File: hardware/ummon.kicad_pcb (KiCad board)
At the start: 4 copper layers, 60 x 60 mm, 84 parts, among them J1 Conn_01x08_Pin, J2 Conn_01x05_Pin, J3 Conn_01x04_Pin, J4 Conn_01x04_Pin, J5 Conn_01x04_Pin, P1 FPC 0.5MM 24P Vertical, Q1 SI1308EDL, SW1 Reboot, SW2 Flash, SW3 Test Button, U1 ESP32-C6-WROOM-1-N8, U2 SCD41-D-R2, U3 SGP41-D-R4, U4 SHT41-AD1B-R2, U5 AMS1117-3.3, U7 SMBJ6.5CA

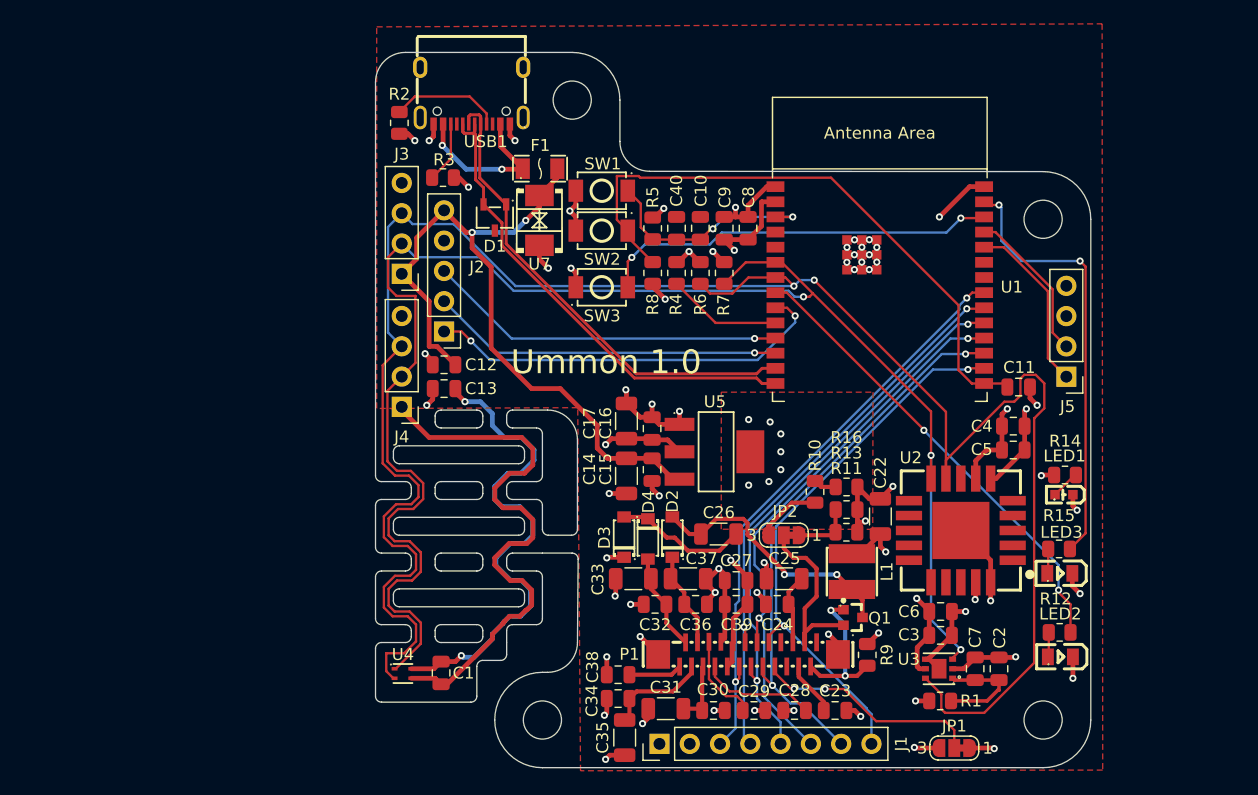
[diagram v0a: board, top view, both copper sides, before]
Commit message: :construction: WIP place ESD parts and route epd charge pump
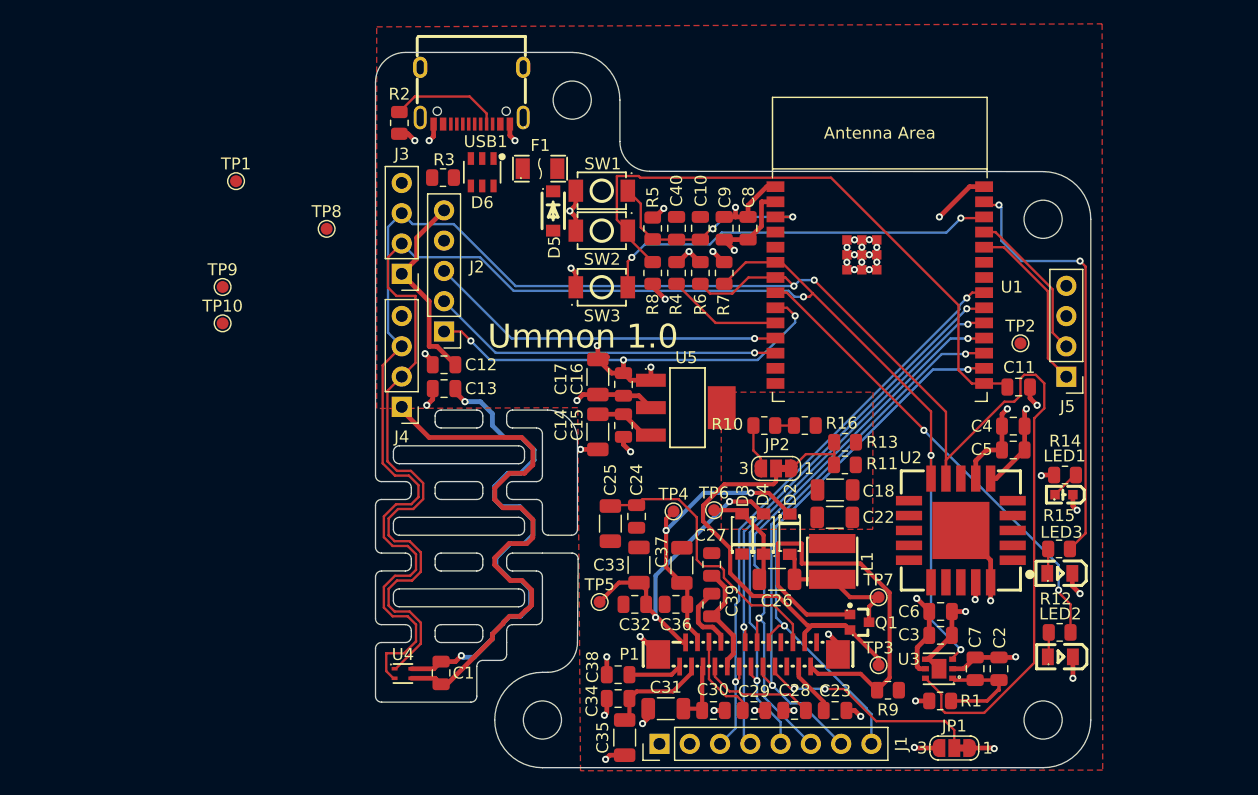
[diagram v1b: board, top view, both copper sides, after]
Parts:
- removed D1: PSM712-LF-T7, parts:SOT-23-3_L3.0-W1.7-P0.95-LS2.9-BR
- removed U7: SMBJ6.5CA, parts:SMB_L4.6-W3.5-LS5.3-BI
- added C18: 22µF, Capacitor_SMD:C_1206_3216Metric, F.Cu at (153.6, 126.7)
- added D5: SMF5.0A, parts:SOD-123F_L2.8-W1.8-LS3.7-RD, F.Cu at (129.9, 103.3)
- added D6: USBLC6-2SC6, parts:SOT-23-6_L2.9-W1.6-P0.95-LS2.8-BL, F.Cu at (124.0, 100.0)
- added TP1: TestPoint, TestPoint:TestPoint_Pad_D1.0mm, F.Cu at (103.3, 100.8)
- added TP10: TestPoint, TestPoint:TestPoint_Pad_D1.0mm, F.Cu at (102.2, 112.7)
- added TP2: TestPoint, TestPoint:TestPoint_Pad_D1.0mm, F.Cu at (169.1, 114.4)
- added TP3: TestPoint, TestPoint:TestPoint_Pad_D1.0mm, F.Cu at (157.2, 141.4)
- added TP4: TestPoint, TestPoint:TestPoint_Pad_D1.0mm, F.Cu at (140.0, 128.5)
- added TP5: TestPoint, TestPoint:TestPoint_Pad_D1.0mm, F.Cu at (133.8, 136.1)
- added TP6: TestPoint, TestPoint:TestPoint_Pad_D1.0mm, F.Cu at (143.4, 128.4)
- added TP7: TestPoint, TestPoint:TestPoint_Pad_D1.0mm, F.Cu at (157.2, 135.7)
- added TP8: TestPoint, TestPoint:TestPoint_Pad_D1.0mm, F.Cu at (110.9, 104.8)
- added TP9: TestPoint, TestPoint:TestPoint_Pad_D1.0mm, F.Cu at (102.2, 109.7)
- moved C25 15.3 mm to (134.7, 129.5), turned to 90 degrees
- moved C24 13.9 mm to (136.9, 128.9), turned to 90 degrees
- moved D3 9.90 mm to (145.8, 130.4)
- moved D2 9.85 mm to (149.8, 130.4), turned to -90 degrees
- moved D4 9.71 mm to (147.6, 130.4), turned to 90 degrees
- moved R10 7.00 mm to (147.6, 121.3), turned to 180 degrees
- moved R16 6.23 mm to (151.0, 121.3)
- moved C26 6.20 mm to (148.7, 134.2), turned to 0 degrees
- moved R11 5.65 mm to (154.4, 124.6)
- moved R13 5.65 mm to (154.4, 122.7)
- moved JP2 5.64 mm to (148.6, 124.9)
- moved C14 4.41 mm to (133.7, 121.8)
- moved C17 4.41 mm to (133.7, 117.2)
- moved U5 4.41 mm to (141.1, 119.8)
- moved C15 4.41 mm to (135.8, 121.3)
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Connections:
- net Net-(D2-A) renamed /EPD_VGH
- net Net-(D3-A) renamed /EPD_VGL
- net Net-(F1-Pad1) renamed /USB_VBUS
- R2 pad 1: Net-(USB1-CC1) -> /USB_CC2
- R3 pad 1: Net-(USB1-CC2) -> /USB_CC1
- USB1 pad A5: Net-(USB1-CC1) -> /USB_CC1
- USB1 pad A6: /USB_D+ -> Net-(USB1-Dp1)
- USB1 pad A7: /USB_D- -> Net-(USB1-Dn1)
- USB1 pad B5: Net-(USB1-CC2) -> /USB_CC2
- USB1 pad B6: /USB_D+ -> Net-(USB1-Dp1)
- USB1 pad B7: /USB_D- -> Net-(USB1-Dn1)
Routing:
- net /USB_D+: track 41.3 -> 0.00 mm
- net /USB_D-: track 40.7 -> 0.00 mm
- net +5V: track 62.0 -> 21.8 mm, vias 2 -> 0
- net GND: track 159.6 -> 134.4 mm, vias 58 -> 46
- net /EPD_GDR: track 12.5 -> 37.7 mm, vias 2 -> 0
- net /EPD_RESE: track 15.5 -> 35.1 mm
- net /EPD_PREVGL: track 8.30 -> 26.3 mm, vias 0 -> 2
- net Net-(C24-Pad2): track 5.93 -> 23.9 mm
- net /EPD_PREVGH: track 8.13 -> 24.7 mm, vias 0 -> 2
- net /USB_VBUS: track 13.9 -> 0.00 mm, vias 2 -> 0
- net /EPD_VGH: track 22.1 -> 12.4 mm, vias 2 -> 0
- net Net-(USB1-CC1): track 9.34 -> 0.00 mm
- net (no net): track 0.00 -> 9.34 mm
- net +3.3V: track 106.7 -> 101.5 mm, vias 22 -> 13
- net Net-(USB1-CC2): track 5.14 -> 0.00 mm
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
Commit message: :zap: Adjust I2C routing between header and SHT41
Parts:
- moved TP1 28.9 mm to (132.1, 99.1)
- moved D6 4.97 mm to (127.2, 103.8)
- moved TP3 1.35 mm to (156.9, 140.1)
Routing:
- net +3.3V: track 101.5 -> 106.3 mm
- net GND: track 134.4 -> 139.1 mm
- net /EPD_RESE: track 35.1 -> 31.2 mm
- net /I2C_SDA: track 133.2 -> 136.3 mm
- net /I2C_SCL: track 170.4 -> 172.5 mm

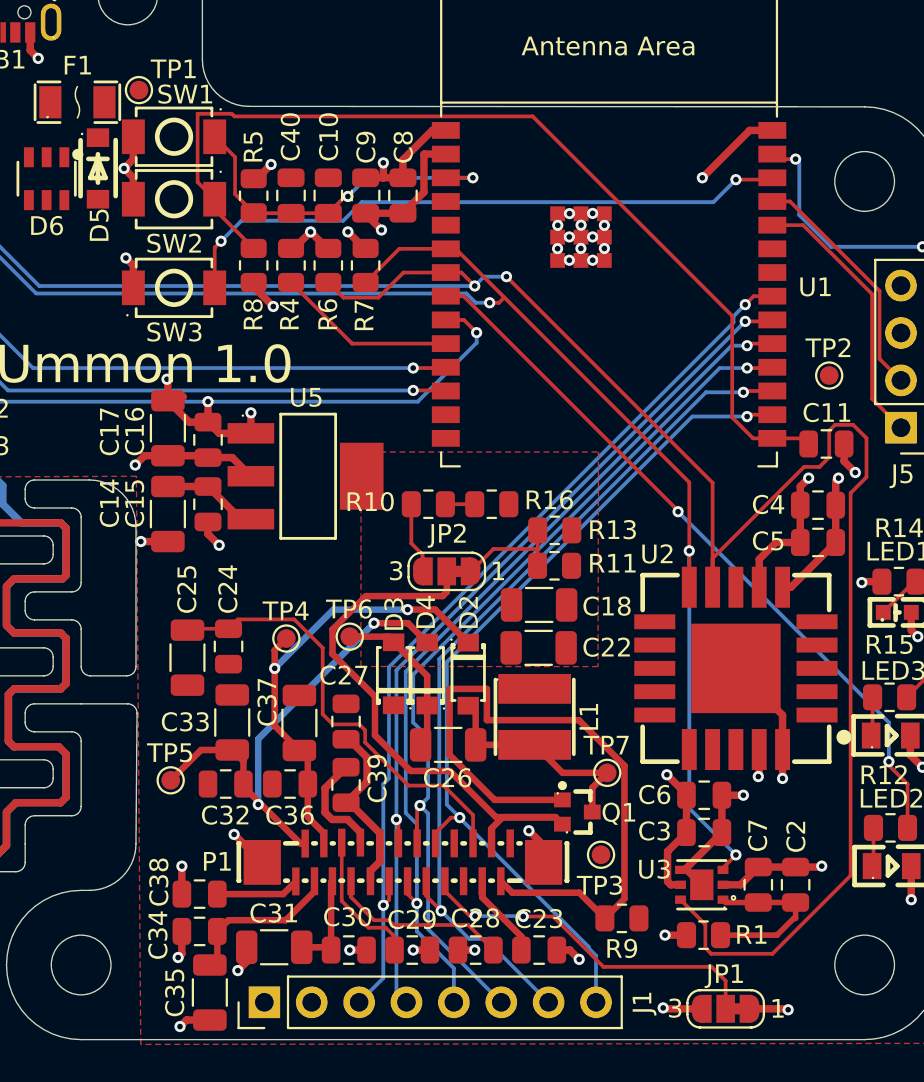
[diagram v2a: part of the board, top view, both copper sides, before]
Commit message: :zap: Rework EPD routing around display connector
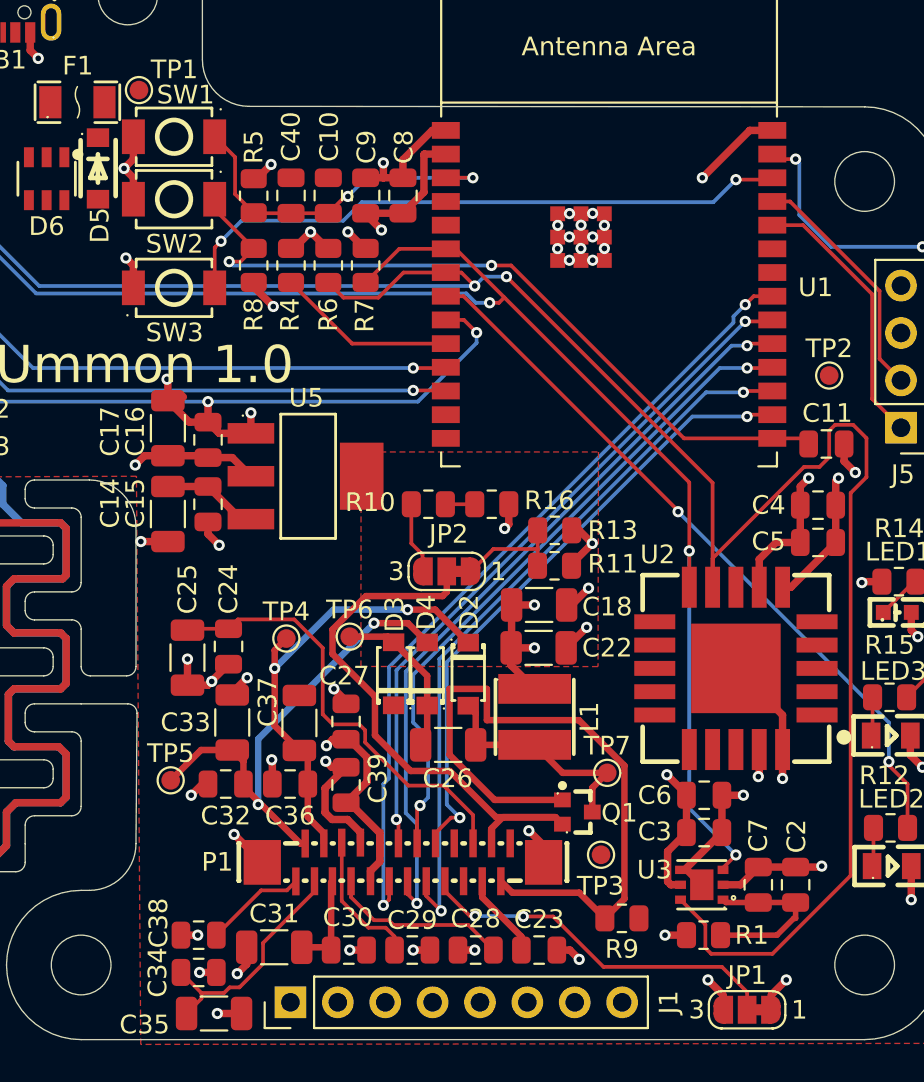
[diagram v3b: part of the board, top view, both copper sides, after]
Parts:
- moved C34 2.20 mm to (135.3, 146.4), turned to 180 degrees
- moved C38 2.20 mm to (135.3, 144.4)
- moved J1 1.40 mm to (140.2, 148.0)
- moved JP1 1.15 mm to (164.7, 148.4)
- moved C35 1.15 mm to (136.1, 148.6), turned to 180 degrees
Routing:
- net GND: track 139.1 -> 155.1 mm, vias 46 -> 57
- net /GPIO9: track 51.7 -> 40.2 mm, vias 0 -> 2
- net +3.3V: track 106.3 -> 114.9 mm, vias 13 -> 16
- net Net-(C34-Pad2): track 8.61 -> 12.5 mm
- net /EPD_RST: track 47.1 -> 48.5 mm
- net /EPD_DC: track 48.0 -> 49.1 mm
- net Net-(C38-Pad2): track 4.49 -> 5.45 mm
- net /EPD_BS: track 19.1 -> 19.9 mm
- net /EPD_CS: track 47.1 -> 47.7 mm
- net /EPD_BUSY: track 46.7 -> 47.3 mm
- net /EPD_SCK: track 47.3 -> 47.9 mm

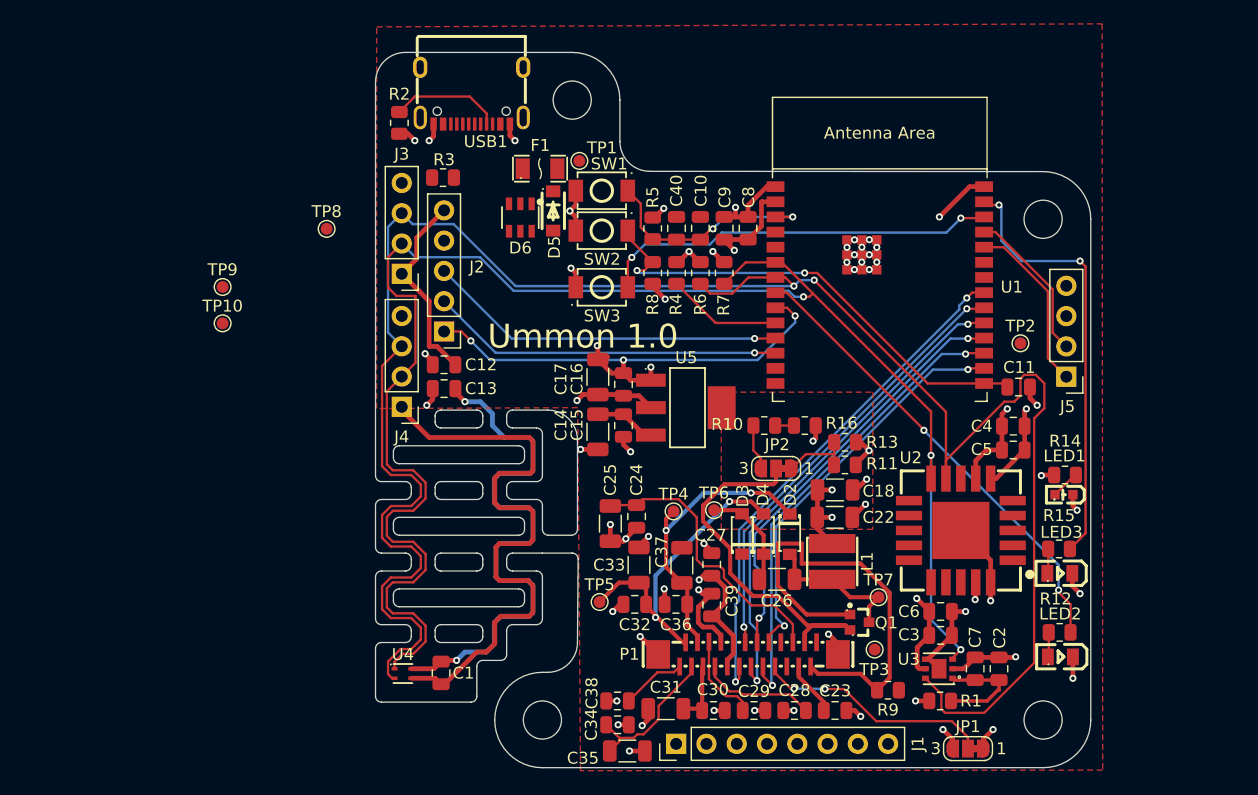
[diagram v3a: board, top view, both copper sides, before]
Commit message: :construction: WIP name USB port data nets and unplace ldo
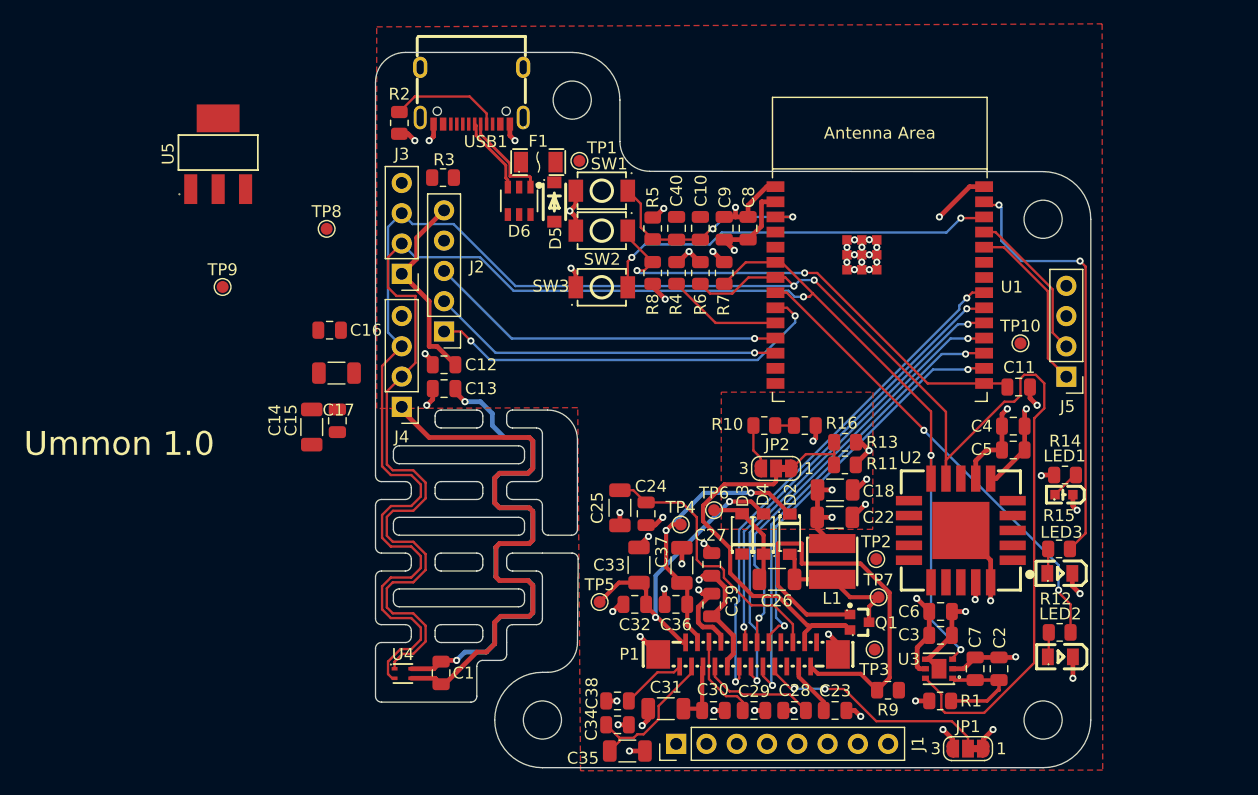
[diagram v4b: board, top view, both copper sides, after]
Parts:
- moved TP2 58.3 mm to (157.0, 132.5)
- moved U5 44.7 mm to (101.8, 98.5), turned to -90 degrees
- moved C16 25.1 mm to (111.2, 113.3), turned to 0 degrees
- moved C15 24.0 mm to (111.8, 120.9)
- moved C14 24.0 mm to (109.7, 121.4)
- moved C17 21.9 mm to (111.7, 116.9), turned to 180 degrees
- moved C25 1.55 mm to (135.5, 128.2)
- moved D6 1.40 mm to (127.0, 102.5)
- moved TP4 1.25 mm to (140.6, 129.6)
- moved C24 0.83 mm to (137.7, 128.7)
- moved D5 0.76 mm to (130.0, 102.5)
- moved F1 0.57 mm to (128.7, 99.2)
- renumbered TP2 to TP10, TP10 to TP2
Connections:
- net Net-(USB1-Dn1) renamed /USB_PORT_D+
- net Net-(USB1-Dp1) renamed /USB_PORT_D-
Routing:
- net GND: track 155.1 -> 143.6 mm, vias 57 -> 53
- net /USB_PORT_D+: track 0.00 -> 7.97 mm
- net +3.3V: track 114.9 -> 107.9 mm, vias 16 -> 15
- net /USB_PORT_D-: track 0.00 -> 6.44 mm
- net +5V: track 21.8 -> 16.7 mm
- net Net-(C24-Pad2): track 23.9 -> 23.1 mm

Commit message: :sparkles: Place ldo and route usb frontend
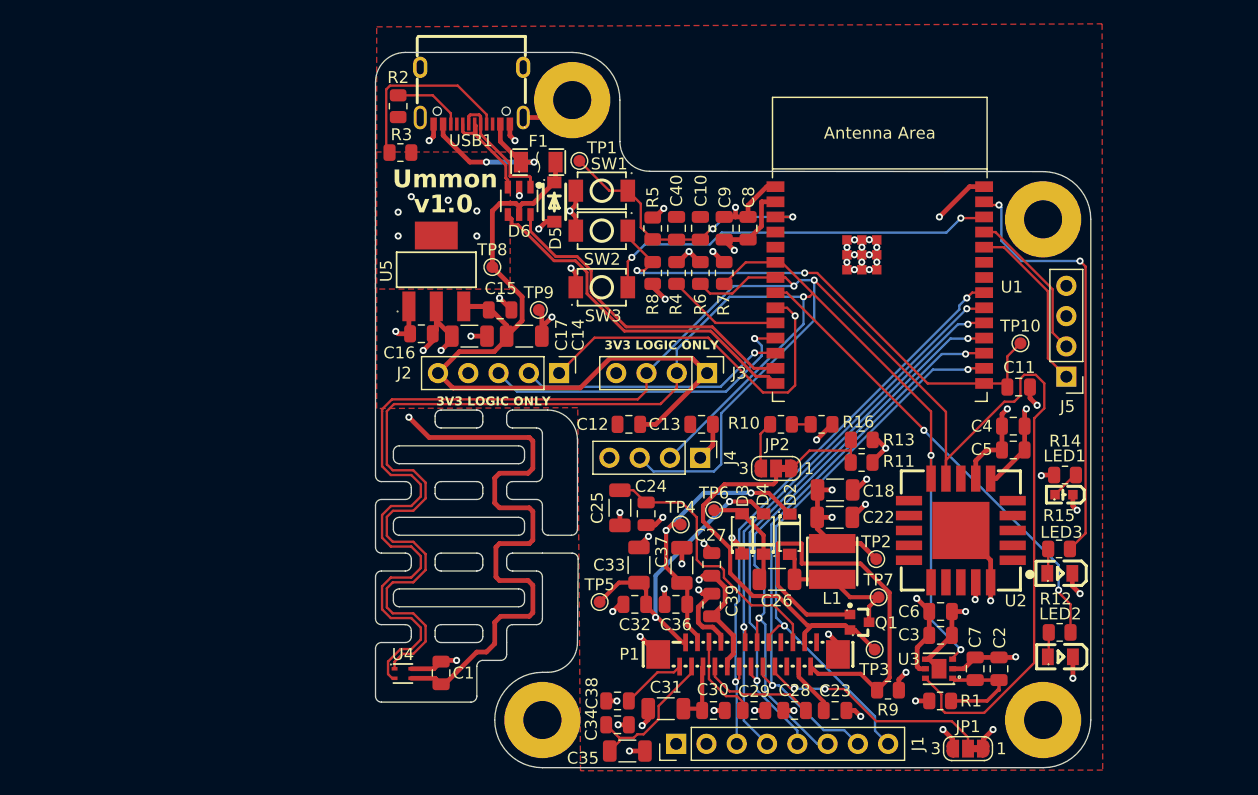
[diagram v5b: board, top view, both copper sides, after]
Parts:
- H1, H2, H3, H4: value MountingHole -> MountingHole_Pad; footprint MountingHole:MountingHole_3.2mm_M3 -> MountingHole:MountingHole_3.2mm_M3_Pad
- moved H3 59.4 mm to (129.0, 146.0)
- moved H1 52.1 mm to (131.5, 94.0)
- moved H2 40.7 mm to (171.0, 104.0)
- moved J3 26.9 mm to (142.8, 116.9), turned to -90 degrees
- moved TP9 26.6 mm to (128.7, 111.6)
- moved J4 25.4 mm to (142.2, 124.0), turned to -90 degrees
- moved C13 21.8 mm to (142.3, 121.2), turned to 180 degrees
- moved U5 20.8 mm to (120.1, 108.3)
- moved C14 19.4 mm to (127.5, 113.8), turned to 0 degrees
- moved C15 16.5 mm to (125.5, 111.6), turned to 0 degrees
- moved C12 16.3 mm to (136.2, 121.2)
- moved TP8 14.3 mm to (124.8, 108.0)
- moved C17 11.6 mm to (122.9, 113.8), turned to 0 degrees
- moved J2 10.3 mm to (130.4, 116.9), turned to -90 degrees
- moved C16 7.71 mm to (118.8, 113.6), turned to 180 degrees
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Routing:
- net +5V: track 16.7 -> 67.5 mm
- net /USB_D+: track 0.00 -> 29.7 mm
- net /USB_D-: track 0.00 -> 27.8 mm
- net GND: track 143.6 -> 162.5 mm, vias 53 -> 58
- net +3.3V: track 107.9 -> 124.5 mm, vias 15 -> 23
- net /USB_CC1: track 0.00 -> 15.8 mm
- net /USB_VBUS: track 0.00 -> 14.5 mm, vias 0 -> 2
- net /I2C_SCL: track 172.5 -> 184.9 mm
- net (no net): track 9.34 -> 0.00 mm
- net /H_RX: track 29.6 -> 22.4 mm
- net /I2C_SDA: track 136.3 -> 142.2 mm
- net /USB_CC2: track 0.00 -> 5.94 mm
- net /EN: track 18.9 -> 24.0 mm
- net /GPIO9: track 40.2 -> 44.4 mm
- net /H_PRESENCE: track 34.2 -> 30.9 mm, vias 2 -> 1
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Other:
- board text added: "3V3 LOGIC ONLY"
- board text added: "Ummon"
- board text added: "v1.0"
- board text removed: "Ummon 1.0"
